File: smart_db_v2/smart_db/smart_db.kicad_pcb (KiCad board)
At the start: 2 copper layers, 4.5 x 13.4 mm, 70 parts, among them J1 AudioJack2, J2 Screw_Terminal_01x02, J3 Conn_01x04_Pin, J4 USB_C_Receptacle_USB2.0_14P, K1 SLA-12VDC-SL-C, Q1 IRLZ44N, Q2 AO3400A, SW1 SW_Push, SW2 SW_Push, SW3 SW_Push, U1 ADS1115IDGS, U2 PC817, U3 AMS1117, U4 ESP32-S3, U5 CP2102N-Axx-xQFN28

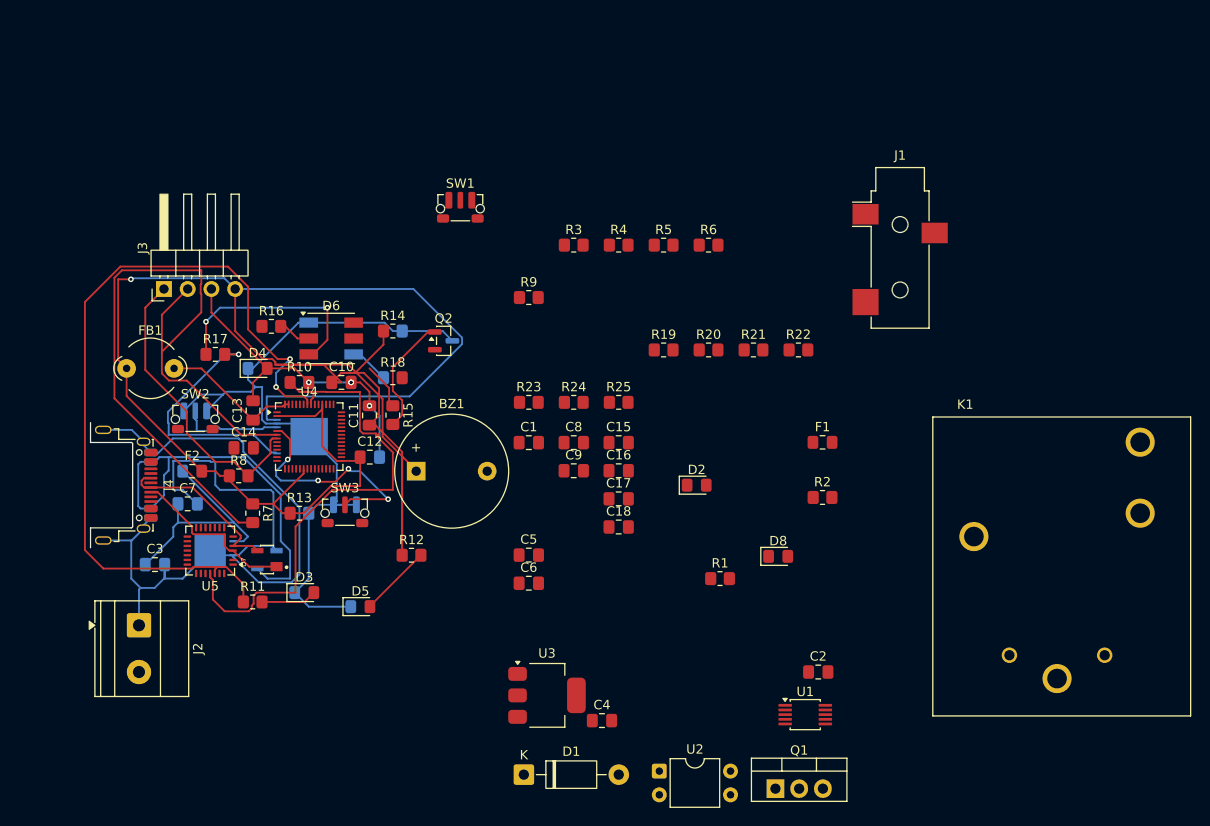
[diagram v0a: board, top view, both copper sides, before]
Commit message: Implement SmartDB v2 firmware, cloud API and documentation
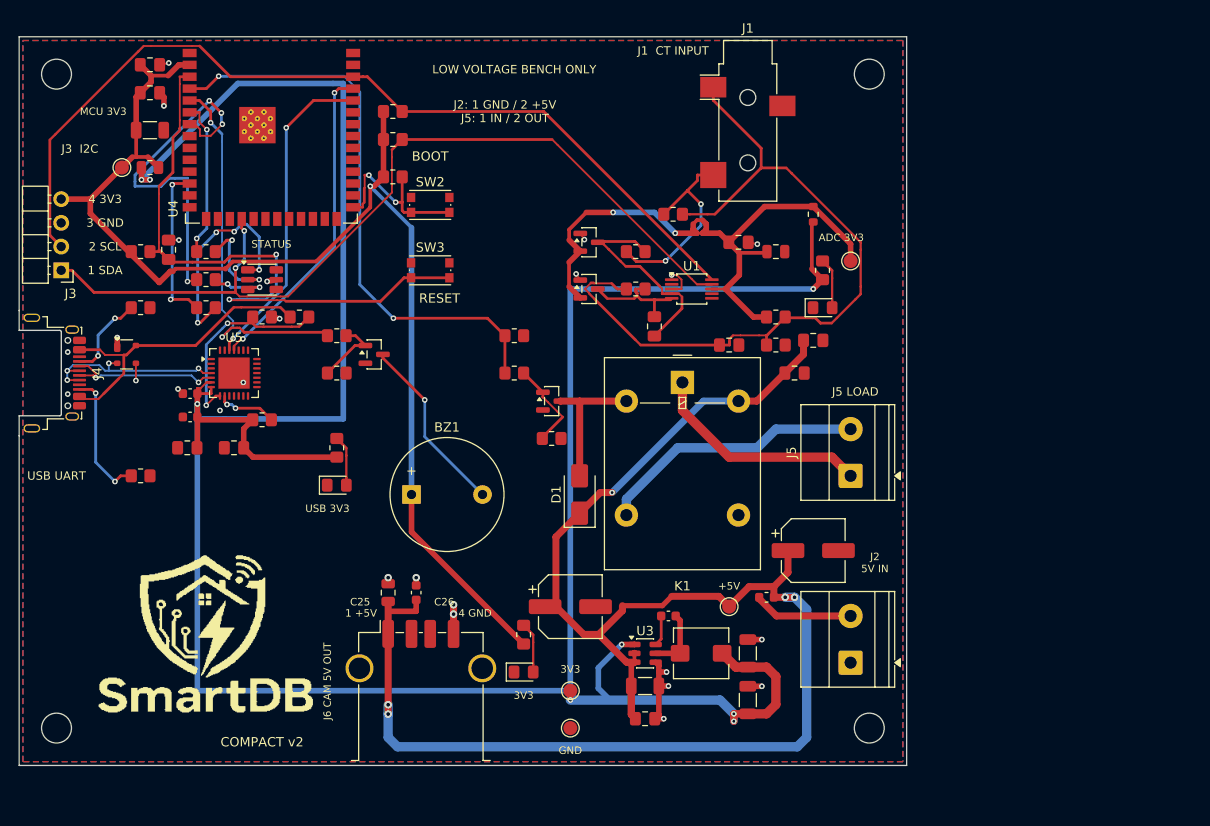
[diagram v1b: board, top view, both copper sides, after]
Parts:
- removed C12, C13, C14: C_US, Capacitor_SMD:C_0805_2012Metric_Pad1.18x1.45mm_HandSolder
- removed D3, D4: LED, LED_SMD:LED_0805_2012Metric_Pad1.15x1.40mm_HandSolder
- removed F2: Fuse, Fuse:Fuse_0805_2012Metric_Pad1.15x1.40mm_HandSolder
- removed FB1: FerriteBead, Ferrite_THT:LairdTech_28C0236-0JW-10
- removed R10, R11: 330, Resistor_SMD:R_0805_2012Metric_Pad1.20x1.40mm_HandSolder
- removed R5: 220, Resistor_SMD:R_0805_2012Metric_Pad1.20x1.40mm_HandSolder
- removed SW1: SW_Push, Button_Switch_SMD:SW_Push_1P1T-MP_NO_Horizontal_Alps_SKRTLAE010
- removed U2: PC817, Package_DIP:DIP-4_W7.62mm
- added C19: 10uF 10V X7R, Capacitor_SMD:C_0805_2012Metric_Pad1.18x1.45mm_HandSolder, F.Cu at (143.0, 83.0)
- added C20: 100nF 10V X7R, Capacitor_SMD:C_0805_2012Metric_Pad1.18x1.45mm_HandSolder, F.Cu at (145.0, 79.5)
- added C21: 100nF 25V X7R, Capacitor_SMD:C_0603_1608Metric, F.Cu at (129.5, 109.0)
- added C22: 100uF 10V, Capacitor_SMD:CP_Elec_6.3x7.7, F.Cu at (119.0, 108.0)
- added C23: 22uF 10V X7R, Capacitor_SMD:C_1206_3216Metric, F.Cu at (74.0, 57.0)
- added C24: 100uF 10V, Capacitor_SMD:CP_Elec_6.3x7.7, F.Cu at (145.0, 102.0)
- added C25: 10uF 16V X7R, Capacitor_SMD:C_0805_2012Metric, F.Cu at (99.5, 106.5)
- added C26: 100nF 16V X7R, Capacitor_SMD:C_0603_1608Metric, F.Cu at (102.5, 106.5)
- added D10: BAT54S, Package_TO_SOT_SMD:SOT-23, F.Cu at (121.0, 74.0)
- added D9: BAT54S, Package_TO_SOT_SMD:SOT-23, F.Cu at (121.0, 69.0)
- added H1: M3 mounting, MountingHole:MountingHole_3.2mm_M3, F.Cu at (64.0, 51.0)
- added H2: M3 mounting, MountingHole:MountingHole_3.2mm_M3, F.Cu at (151.0, 51.0)
- added H3: M3 mounting, MountingHole:MountingHole_3.2mm_M3, F.Cu at (64.0, 121.0)
- added H4: M3 mounting, MountingHole:MountingHole_3.2mm_M3, F.Cu at (151.0, 121.0)
- added J5: TEST_LOAD, TerminalBlock_Phoenix:TerminalBlock_Phoenix_MKDS-1,5-2_1x02_P5.00mm_Horizontal, F.Cu at (149.0, 94.0)
- added J6: CAM USB 5V OUT, SmartDB:USB_A_TE_292303-7_Horizontal_Edge, F.Cu at (103.0, 117.3)
- added L1: 6.8uH SRP5030TA-6R8M, Inductor_SMD:L_Bourns_SRP5030T, F.Cu at (133.0, 113.0)
- added R26: 100k, Resistor_SMD:R_0805_2012Metric_Pad1.20x1.40mm_HandSolder, F.Cu at (94.0, 83.0)
- added R27: 100k, Resistor_SMD:R_0805_2012Metric_Pad1.20x1.40mm_HandSolder, F.Cu at (113.0, 79.0)
- added R28: 100k, Resistor_SMD:R_0805_2012Metric_Pad1.20x1.40mm_HandSolder, F.Cu at (117.0, 90.0)
- added R29: 0R 1A min, Resistor_SMD:R_0805_2012Metric, F.Cu at (74.0, 61.0)
- added R30: 10R 1%, Resistor_SMD:R_0603_1608Metric, F.Cu at (145.0, 66.0)
- added TP1: LOGIC_5V_FUSED, TestPoint:TestPoint_Pad_D1.5mm, F.Cu at (136.0, 108.0)
- added TP2: VCC, TestPoint:TestPoint_Pad_D1.5mm, F.Cu at (119.0, 117.0)
- added TP3: MCU_3V3, TestPoint:TestPoint_Pad_D1.5mm, F.Cu at (71.0, 61.0)
- added TP4: ADC_3V3, TestPoint:TestPoint_Pad_D1.5mm, F.Cu at (149.0, 71.0)
- added TP5: BGND, TestPoint:TestPoint_Pad_D1.5mm, F.Cu at (119.0, 121.0)
- BZ1: value Buzzer -> Buzzer (3V3 type TBD)
- C1: value 100nF -> 220nF
- C10: value C_US -> 100nF
- C11: value C_US -> 1uF
- C15, C18: value 0.1uF -> 100nF; footprint Capacitor_SMD:C_0805_2012Metric_Pad1.18x1.45mm_HandSolder -> Capacitor_SMD:C_0603_1608Metric
- C4: value 1uF -> 10uF 10V X7R; footprint Capacitor_SMD:C_0805_2012Metric_Pad1.18x1.45mm_HandSolder -> Capacitor_SMD:C_0805_2012Metric
- C5: value C_US -> 10uF 10V X7R; footprint Capacitor_SMD:C_0805_2012Metric_Pad1.18x1.45mm_HandSolder -> Capacitor_SMD:C_1206_3216Metric
- C6: value C_US -> 100nF 10V X7R
- C7, C8: value C_US -> 22uF 10V X7R; footprint Capacitor_SMD:C_0805_2012Metric_Pad1.18x1.45mm_HandSolder -> Capacitor_SMD:C_1206_3216Metric
- C9: value C_US -> 10uF
- D1: value 1N4007 -> M7 (1N4007 SMD); footprint Diode_THT:D_DO-41_SOD81_P10.16mm_Horizontal -> Diode_SMD:D_SMA
- D2: value LED -> ADC POWER
- D5: value LED -> POWER
- D6: value LED_KRGB -> SMLVN6RGB1U1; footprint LED_SMD:LED_RGB_5050-6 -> SmartDB:LED_ROHM_SMLVN6_Preview
- D7: footprint rpi:SOT143 -> Package_TO_SOT_SMD:SOT-143
- D8: value LED -> USB BRIDGE POWER
- F1: value Polyfuse -> 046701.5NRHF 1.5A; footprint Fuse:Fuse_0805_2012Metric_Pad1.15x1.40mm_HandSolder -> Fuse:Fuse_0603_1608Metric
- J1: value AudioJack2 -> SCT-013-000 ONLY; footprint Connector_Audio:Jack_3.5mm_CUI_SJ-3523-SMT_Horizontal -> SmartDB:Jack_3.5mm_SJ-3523-SMT_Local
- J2: value Screw_Terminal_01x02 -> REGULATED 5V INPUT
- J3: value Conn_01x04_Pin -> THERMAL_I2C; footprint Connector_PinHeader_2.54mm:PinHeader_1x04_P2.54mm_Horizontal -> SmartDB:PinHeader_1x04_P2.54mm_Horizontal_Edge
- J4: footprint Connector_USB:USB_C_Receptacle_Amphenol_12401948E412A -> SmartDB:USB_C_Receptacle_Amphenol_12401948E412A_Preview
- K1: value SLA-12VDC-SL-C -> G5LE-1 DC5; footprint rpi:RELAY_SLA-12VDC-SL-C -> Relay_THT:Relay_SPDT_Omron-G5LE-1
- Q1: value IRLZ44N -> AO3400A; footprint Package_TO_SOT_THT:TO-220-3_Vertical -> Package_TO_SOT_SMD:SOT-23
- R1, R2: value 10k -> 1k 1%
- R13, R14: value R_US -> 10k
- R15: value R -> 100
- R21: value R_US -> 1k
- R23: value 33 -> 18 ohm 1% 0.25W
- R3, R4: value 10k -> 10k 1%
- SW2: value SW_Push -> BOOT; footprint Button_Switch_SMD:SW_Push_1P1T-MP_NO_Horizontal_Alps_SKRTLAE010 -> Button_Switch_SMD:SW_Push_1P1T_NO_CK_KMR2
- SW3: value SW_Push -> RESET; footprint Button_Switch_SMD:SW_Push_1P1T-MP_NO_Horizontal_Alps_SKRTLAE010 -> Button_Switch_SMD:SW_Push_1P1T_NO_CK_KMR2
- U3: value AMS1117 -> AP63203WU-7; footprint Package_TO_SOT_SMD:SOT-223-3_TabPin2 -> Package_TO_SOT_SMD:TSOT-23-6
- U4: value ESP32-S3 -> ESP32-S3-WROOM-1-N16R8; footprint Package_DFN_QFN:QFN-56-1EP_7x7mm_P0.4mm_EP4x4mm -> SmartDB:ESP32_S3_WROOM_1_Edge
- U5: value CP2102N-Axx-xQFN28 -> CP2102N-A02-GQFN28
- moved J2 76.3 mm to (149.0, 114.0), turned to 90 degrees
- moved C3 71.4 mm to (137.0, 69.0)
- moved C9 62.8 mm to (74.0, 50.0)
- moved C7 62.1 mm to (138.0, 113.0), turned to 90 degrees
- moved C4 53.5 mm to (141.0, 70.0)
- moved R21 53.1 mm to (86.0, 88.0)
- moved R25 51.8 mm to (73.0, 94.0)
- moved R22 50.5 mm to (94.0, 91.0), turned to 90 degrees
- moved R20 47.9 mm to (86.0, 77.0)
- moved Q1 47.9 mm to (117.0, 86.0)
- moved D8 47.9 mm to (94.0, 95.0)
- moved R24 47.5 mm to (73.0, 76.0)
- moved C18 47.4 mm to (78.3, 87.7), turned to 180 degrees
- moved U1 47.2 mm to (132.0, 74.0)
- moved C16 46.2 mm to (78.0, 91.0), turned to 180 degrees
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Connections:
- net Net-(D2-A) renamed ADC_LED_A
- net Net-(D6-RA) renamed LED_R_A
- net Net-(D8-A) renamed USB_LED_A
- net Net-(Q1-G) renamed RELAY_GATE
- net Net-(U5-D-) renamed USB_D-
- net Net-(U5-~{RST}) renamed USB_RESET
- BZ1 pad 1: Net-(BZ1-+) -> MCU_3V3
- BZ1 pad 2: Net-(BZ1--) -> BUZZER_LOW
- C1 pad 1: PVCC -> ADC_AIN0
- C1 pad 2: PGND -> ADC_AIN1
- C10 pad 1: Net-(BZ1-+) -> MCU_3V3
- C10 pad 2: Net-(D4-A) -> BGND
- C11 pad 1: Net-(BZ1-+) -> EN
- C11 pad 2: Net-(D4-A) -> BGND
- C15 pad 1: Net-(U5-VREGIN) -> VCC
- C16 pad 1: Net-(U5-VREGIN) -> VCC
- C17 pad 1: Net-(C17-Pad1) -> VCC
- C17 pad 2: VCC -> BGND
- C18 pad 1: Net-(C17-Pad1) -> VCC
- C18 pad 2: VCC -> BGND
- C2 pad 1: Net-(U1-AIN1) -> CT_BIAS
- C2 pad 2: PGND -> BGND
- C3 pad 1: VCC -> ADC_3V3
- C4 pad 1: VCC -> ADC_3V3
- C5 pad 1: Net-(U3-VI) -> LOGIC_5V_FUSED
- C6 pad 1: Net-(U3-VI) -> LOGIC_5V_FUSED
- C9 pad 1: Net-(BZ1-+) -> MCU_3V3
- C9 pad 2: Net-(D4-A) -> BGND
- D1 pad 1: Net-(D1-K) -> LOGIC_5V_FUSED
- D1 pad 2: Net-(D1-A) -> RELAY_LOW
- D5 pad 1: IO0 -> BGND
- D6 pad 1: IO0 -> LED_B_A
- D6 pad 3: Net-(D6-GA) -> LED_G_A
- D6 pad 4: Net-(D6-BA) -> BGND
- D6 pad 5: (no net) -> BGND
- D6 pad 6: (no net) -> BGND
- D7 pad 1: Net-(U5-D+) -> BGND
- D7 pad 2: BGND -> USB_D+
- D7 pad 4: Net-(U5-VBUS) -> USB_VBUS
- F1 pad 1: Net-(F1-Pad1) -> LOGIC_5V_IN
- F1 pad 2: Net-(U3-VI) -> LOGIC_5V_FUSED
- J1 pad S: PVCC -> CT_BIAS
- J1 pad T: PGND -> CT_HI
- J2 pad 2: BVCC -> LOGIC_5V_IN
- J3 pad 3: Net-(D4-A) -> BGND
- J3 pad 4: Net-(BZ1-+) -> MCU_3V3
- J4 pad A4: Net-(U5-VBUS) -> USB_VBUS
- J4 pad A5: Net-(J4-CC1) -> USB_CC1
- J4 pad A6: Net-(U5-D+) -> USB_D+
- J4 pad A9: Net-(U5-VBUS) -> USB_VBUS
- J4 pad B4: Net-(U5-VBUS) -> USB_VBUS
- J4 pad B5: Net-(J4-CC2) -> USB_CC2
- J4 pad B6: Net-(U5-D+) -> USB_D+
- J4 pad B9: Net-(U5-VBUS) -> USB_VBUS
- Q1 pad 2: Net-(D1-K) -> BGND
- Q1 pad 3: BGND -> RELAY_LOW
- Q2 pad 2: Net-(BZ1--) -> BGND
- Q2 pad 3: IO0 -> BUZZER_LOW
- R1 pad 1: Net-(U1-AIN0) -> CT_HI
- R1 pad 2: PVCC -> ADC_AIN0
- R12 pad 1: Net-(BZ1-+) -> MCU_3V3
- R13 pad 1: Net-(BZ1-+) -> MCU_3V3
- R13 pad 2: IO0 -> EN
- R14 pad 1: Net-(BZ1-+) -> MCU_3V3
- R14 pad 2: IO0 -> BOOT
- R15 pad 1: Net-(U4-GPIO5) -> BUZZER_DRIVE
- R16 pad 1: Net-(U4-GPIO6) -> LED_R
- R17 pad 1: Net-(D6-GA) -> LED_G
- R17 pad 2: Net-(U4-GPIO7) -> LED_G_A
- R18 pad 1: Net-(D6-BA) -> LED_B
- R18 pad 2: Net-(U4-GPIO8) -> LED_B_A
- R19 pad 1: Net-(U5-VREGIN) -> USB_VBUS
- R19 pad 2: Net-(U5-VBUS) -> USB_VBUS_SENSE
- R2 pad 1: Net-(U1-AIN0) -> CT_BIAS
- R2 pad 2: Net-(U1-AIN1) -> ADC_AIN1
- R20 pad 1: Net-(U5-VBUS) -> USB_VBUS_SENSE
- R22 pad 1: Net-(C17-Pad1) -> VCC
- R23 pad 1: PVCC -> CT_HI
- R23 pad 2: PGND -> CT_BIAS
- R24 pad 1: BGND -> USB_CC1
- R24 pad 2: Net-(J4-CC2) -> BGND
- R25 pad 1: BGND -> USB_CC2
- R25 pad 2: Net-(J4-CC1) -> BGND
- R3 pad 1: VCC -> ADC_3V3
- R3 pad 2: BGND -> CT_BIAS
- R4 pad 1: VCC -> CT_BIAS
- R6 pad 1: Net-(R6-Pad1) -> CTL
- R7 pad 1: Net-(BZ1-+) -> MCU_3V3
- R8 pad 1: Net-(BZ1-+) -> MCU_3V3
- SW2 pad 1: IO0 -> BGND
- SW2 pad 2: Net-(U4-GPIO0) -> BOOT
- SW3 pad 1: IO0 -> BGND
- SW3 pad 2: Net-(U4-GPIO1) -> EN
- U1 pad 1: PGND -> BGND
- U1 pad 2: PGND -> unconnected-(U1-ALERT/RDY-Pad2)
- U1 pad 4: Net-(U1-AIN0) -> ADC_AIN0
- U1 pad 5: Net-(U1-AIN1) -> ADC_AIN1
- U1 pad 6: PGND -> BGND
- U1 pad 7: PGND -> BGND
- U1 pad 8: VCC -> ADC_3V3
- U3 pad 1: BGND -> VCC
- U3 pad 2: VCC -> LOGIC_5V_FUSED
- U3 pad 3: Net-(U3-VI) -> LOGIC_5V_FUSED
- U4 pad 1: unconnected-(U4-LNA_IN-Pad1) -> BGND
- U4 pad 10: Net-(U4-GPIO5) -> unconnected-(U4-IO17-Pad10)
- U4 pad 11: Net-(U4-GPIO6) -> unconnected-(U4-IO18-Pad11)
- U4 pad 12: Net-(U4-GPIO7) -> LED_B
- U4 pad 13: Net-(U4-GPIO8) -> unconnected-(U4-USB_D--Pad13)
- U4 pad 18: unconnected-(U4-GPIO13-Pad18) -> SDA
- U4 pad 2: Net-(BZ1-+) -> MCU_3V3
- U4 pad 20: Net-(BZ1-+) -> unconnected-(U4-IO12-Pad20)
- U4 pad 27: unconnected-(U4-GPIO21-Pad27) -> BOOT
- U4 pad 29: Net-(BZ1-+) -> unconnected-(U4-IO36-Pad29)
- U4 pad 3: Net-(BZ1-+) -> EN
- U4 pad 36: unconnected-(U4-SPICLK_N-Pad36) -> TX
- U4 pad 37: unconnected-(U4-SPICLK_P-Pad37) -> RX
- U4 pad 38: unconnected-(U4-GPIO33-Pad38) -> SCL
- U4 pad 4: IO0 -> CTL
- U4 pad 40: unconnected-(U4-GPIO35-Pad40) -> BGND
- U4 pad 41: unconnected-(U4-GPIO36-Pad41) -> BGND
- U4 pad 5: Net-(U4-GPIO0) -> BUZZER_DRIVE
- U4 pad 6: Net-(U4-GPIO1) -> LED_R
- U4 pad 7: SCL -> LED_G
- U4 pad 8: SDA -> unconnected-(U4-IO15-Pad8)
- U4 pad 9: CTL -> unconnected-(U4-IO16-Pad9)
- U5 pad 4: Net-(U5-D+) -> USB_D+
- U5 pad 7: Net-(U5-VREGIN) -> VCC
- U5 pad 8: Net-(U5-VBUS) -> USB_VBUS_SENSE
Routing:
- net VCC: track 25.7 -> 305.1 mm, vias 0 -> 8
- net Net-(BZ1-+): track 220.4 -> 0.00 mm, vias 1 -> 0
- net LOGIC_5V_FUSED: track 0.00 -> 178.5 mm, vias 0 -> 5
- net MCU_3V3: track 0.00 -> 133.1 mm, vias 0 -> 1
- net CT_BIAS: track 0.00 -> 82.0 mm
- net IO0: track 79.0 -> 0.00 mm
- net BGND: track 104.7 -> 29.3 mm, vias 0 -> 24
- net EN: track 0.00 -> 70.2 mm, vias 0 -> 2
- net ADC_3V3: track 0.00 -> 65.7 mm, vias 0 -> 2
- net SDA: track 32.1 -> 95.2 mm, vias 0 -> 2
- net CTL: track 0.00 -> 61.9 mm, vias 0 -> 2
- net TX: track 87.2 -> 34.7 mm
- net Net-(U5-VBUS): track 44.3 -> 0.00 mm
- net BUZZER_DRIVE: track 0.00 -> 40.4 mm, vias 0 -> 2
- net LED_G: track 0.00 -> 38.5 mm, vias 0 -> 4
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- added copper zone on B.Cu, net BGND
- added copper zone on F.Cu, net BGND
- added copper zone on In1.Cu, net BGND
- added copper zone on In2.Cu, net BGND
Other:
- board size 4.5 x 13.4 mm -> 95 x 78 mm
- copper layers 2 -> 4
- board text added: "+5V"
- board text added: "1 +5V"
- board text added: "1 GND"
- board text added: "1 IN"
- board text added: "1 SDA"
- board text added: "2 +5V"
- board text added: "2 OUT"
- board text added: "2 SCL"
- board text added: "3 GND"
- board text added: "3V3"
- board text added: "4 3V3"
- board text added: "4 GND"
- board text added: "ADC 3V3"
- board text added: "BOOT"
- board text added: "C25"
- board text added: "C26"
- board text added: "COMPACT v2"
- board text added: "GND"
- board text added: "J1 CT INPUT"
- board text added: "J1 SCT-013-000 ONLY TIP: CT_HI / SLEEVE: CT_BIAS"
- board text added: "J2 5V IN"
- board text added: "J2 REGULATED 5V"
- board text added: "J2: 1 GND / 2 +5V J5: 1 IN / 2 OUT"
- board text added: "J3 I2C"
- board text added: "J3 I2C / 3.3V"
- board text added: "J4 USB UART SELF-POWERED / NO USB SUPPLY"
- board text added: "J5 LOAD"
- board text added: "J5 RELAY / N.O."
- board text added: "J6 CAM 5V OUT"
- board text added: "J6 CAM 5V OUT 1 +5V / 4 GND 2,3 NC / SH GND"
- board text added: "LOW VOLTAGE BENCH ONLY"
- board text added: "MCU 3V3"
- board text added: "RESET"
- board text added: "SMARTDB COMPACT v2 LOW VOLTAGE BENCH PROTOTYPE"
- board text added: "STATUS"
- board text added: "USB 3V3"
- board text added: "USB UART"
